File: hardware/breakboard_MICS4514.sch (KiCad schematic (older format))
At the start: 11 parts, among them J1 outputs, Q1 2N7002, U1 TLC2272, U2 MICS-4514

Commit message: shape of edge cuts
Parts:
- removed J1: outputs, Connector_PinHeader_2.54mm:PinHeader_1x07_P2.54mm_Vertical, symbol Connector:Conn_01x07_Female
- added J1: OUTPUTS, Connector_PinHeader_2.54mm:PinHeader_1x05_P2.54mm_Vertical, symbol Connector:Conn_01x05_Female
- R5: value 22k -> 269
- U2: symbol electroniccats:MICS-4514 -> breakboard_MICS4514-rescue:MICS-4514-electroniccats
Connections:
- wire segments 55 -> 50
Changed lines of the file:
@@
 EESchema Schematic File Version 4
 LIBS:breakboard_MICS4514-cache
-EELAYER 26 0
+EELAYER 29 0
 EELAYER END
 $Descr A4 11693 8268
@@
 $EndDescr
 $Comp
-L electroniccats:MICS-4514 U2
+L breakboard_MICS4514-rescue:MICS-4514-electroniccats U2
 U 1 1 5C5C9644
 P 6730 2780
@@
 P 5190 3310
 F 0 "R5" H 5260 3356 50  0000 L CNN
-F 1 "22k" H 5260 3265 50  0000 L CNN
+F 1 "269" H 5260 3265 50  0000 L CNN
 F 2 "Resistor_SMD:R_0805_2012Metric_Pad1.15x1.40mm_HandSolder" V 5120 3310 50  0001 C CNN
 F 3 "https://www.mouser.mx/datasheet/2/348/esr-e-1139161.pdf" H 5190 3310 50  0001 C CNN
@@
 	6980 5040 7080 5040
 $Comp
-L Connector:Conn_01x07_Female J1
-U 1 1 5C5D8712
-P 7760 3800
-F 0 "J1" H 7788 3826 50  0000 L CNN
-F 1 "outputs" H 7788 3735 50  0000 L CNN
-F 2 "Connector_PinHeader_2.54mm:PinHeader_1x07_P2.54mm_Vertical" H 7760 3800 50  0001 C CNN
-F 3 "~" H 7760 3800 50  0001 C CNN
-	1    7760 3800
-	1    0    0    -1
-$EndComp
-$Comp
 L power:+3V3 #PWR08
 U 1 1 5C5D9752
-P 6830 3420
-F 0 "#PWR08" H 6830 3270 50  0001 C CNN
-F 1 "+3V3" H 6845 3593 50  0000 C CNN
-F 2 "" H 6830 3420 50  0001 C CNN
-F 3 "" H 6830 3420 50  0001 C CNN
-	1    6830 3420
+P 7070 3640
+F 0 "#PWR08" H 7070 3490 50  0001 C CNN
+F 1 "+3V3" H 7085 3813 50  0000 C CNN
+F 2 "" H 7070 3640 50  0001 C CNN
+F 3 "" H 7070 3640 50  0001 C CNN
+	1    7070 3640
 	1    0    0    -1
 $EndComp
@@
 L power:GND #PWR07
 U 1 1 5C5D97A5
-P 6830 3740
-F 0 "#PWR07" H 6830 3490 50  0001 C CNN
-F 1 "GND" H 6835 3567 50  0000 C CNN
-F 2 "" H 6830 3740 50  0001 C CNN
-F 3 "" H 6830 3740 50  0001 C CNN
-	1    6830 3740
-	1    0    0    -1
-$EndComp
-Text Label 7460 3600 2    50   ~ 0
+P 7070 3820
+F 0 "#PWR07" H 7070 3570 50  0001 C CNN
+F 1 "GND" H 7075 3647 50  0000 C CNN
+F 2 "" H 7070 3820 50  0001 C CNN
+F 3 "" H 7070 3820 50  0001 C CNN
+	1    7070 3820
+	1    0    0    -1
+$EndComp
+Text Label 7310 4100 2    50   ~ 0
 PRE_HEALTING
-Text Label 7460 3800 2    50   ~ 0
-OX
-Text Label 7460 3900 2    50   ~ 0
-RED
-Text Label 7460 4100 2    50   ~ 0
+Text Label 7310 4000 2    50   ~ 0
 NO2
-Text Label 7460 4000 2    50   ~ 0
+Text Label 7310 3900 2    50   ~ 0
 CO2
 Wire Wire Line
-	7460 3600 7560 3600
-Wire Wire Line
-	7460 3800 7560 3800
-Wire Wire Line
-	7460 3900 7560 3900
-Wire Wire Line
-	7460 4000 7560 4000
-Wire Wire Line
-	7460 4100 7560 4100
-Wire Wire Line
 	5190 3820 5190 3460
 Wire Wire Line
 	4870 3820 4870 3460
-Wire Wire Line
-	6830 3740 6830 3700
-Wire Wire Line
-	6830 3700 7560 3700
-Wire Wire Line
-	7560 3500 6830 3500
-Wire Wire Line
-	6830 3500 6830 3420
 Text Label 6080 4940 2    50   ~ 0
 RED
+$Comp
+L Connector:Conn_01x05_Female J1
+U 1 1 5CFFB1C2
+P 7510 3900
+F 0 "J1" H 7538 3926 50  0000 L CNN
+F 1 "OUTPUTS" H 7538 3835 50  0000 L CNN
+F 2 "Connector_PinHeader_2.54mm:PinHeader_1x05_P2.54mm_Vertical" H 7510 3900 50  0001 C CNN
+F 3 "~" H 7510 3900 50  0001 C CNN
+	1    7510 3900
+	1    0    0    -1
+$EndComp
+Wire Wire Line
+	7070 3640 7070 3700
+Wire Wire Line
+	7070 3700 7310 3700
+Wire Wire Line
+	7310 3800 7070 3800
+Wire Wire Line
+	7070 3800 7070 3820
 $EndSCHEMATC

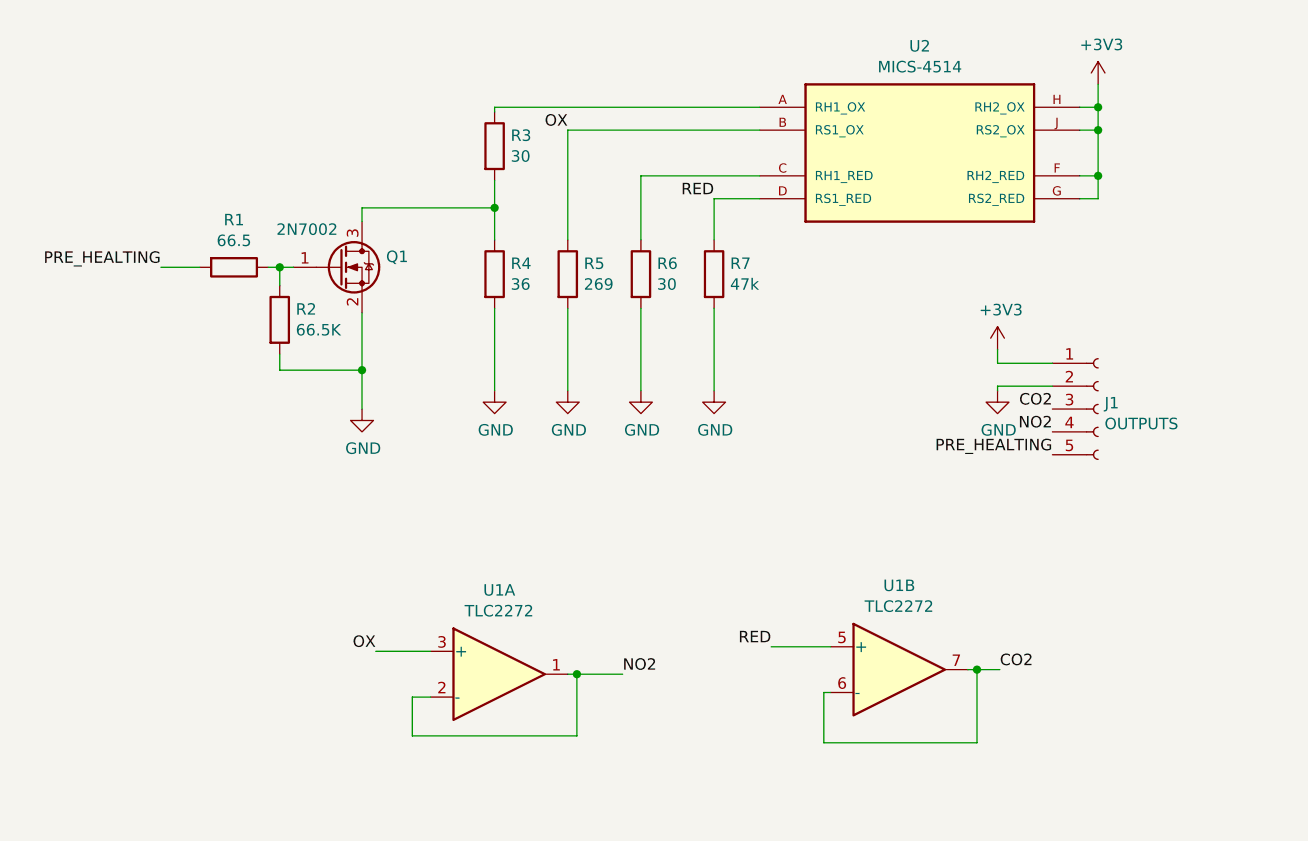
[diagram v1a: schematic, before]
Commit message: Add voltage pins for opamp, add decoupling caps, new component placement
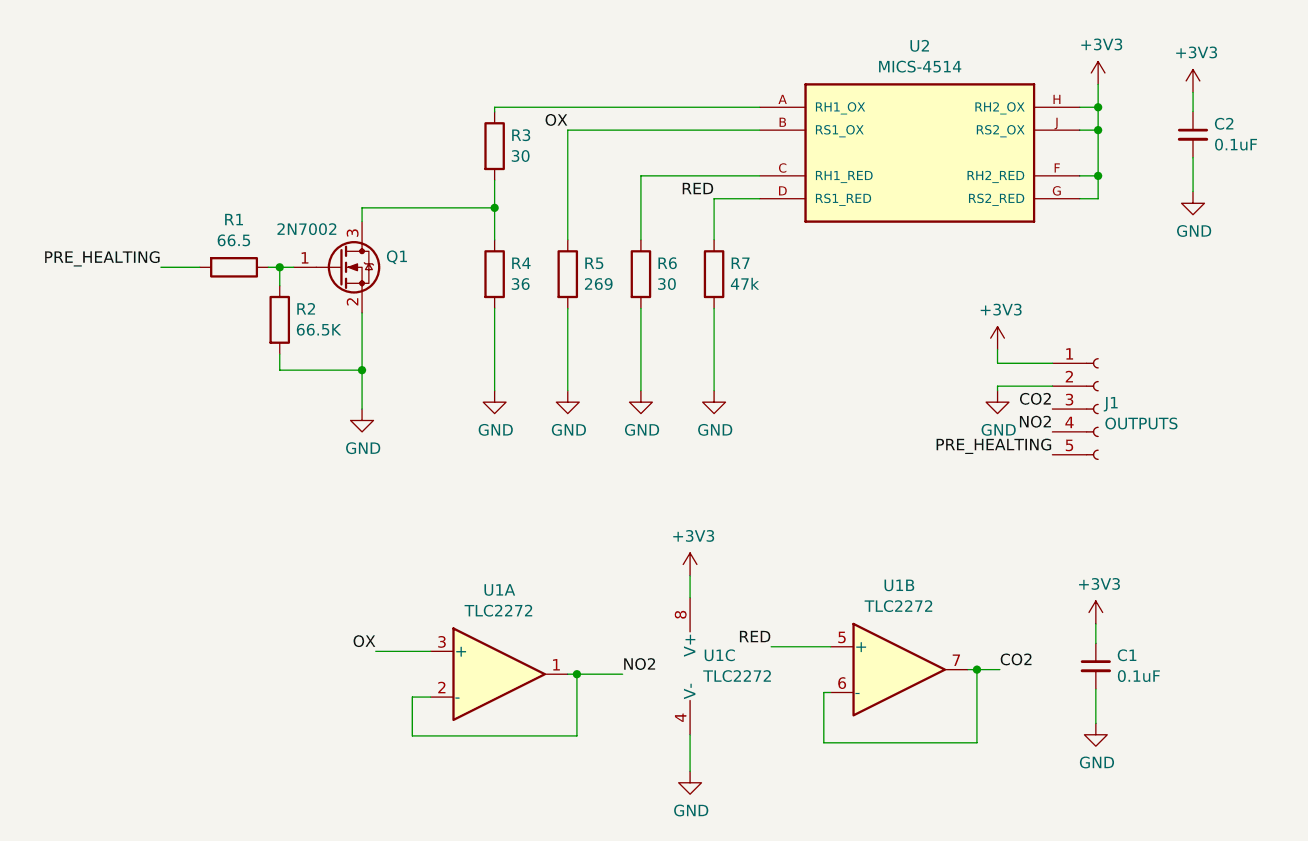
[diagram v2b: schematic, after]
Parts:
- added C1, C2: 0.1uF, Capacitor_SMD:C_0805_2012Metric_Pad1.15x1.40mm_HandSolder, symbol Device:C_Small
- added unit 3 of U1
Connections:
- net +3V3: now also C1.1, C2.1, U1.8 (V+)
- net GND: now also C1.2, C2.2, U1.4 (V-)
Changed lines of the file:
@@
 EESchema Schematic File Version 4
-LIBS:breakboard_MICS4514-cache
-EELAYER 29 0
+EELAYER 30 0
 EELAYER END
 $Descr A4 11693 8268
@@
 Sheet 1 1
 Title "Breakboard MICS4514"
-Date "2019-02-07"
-Rev ""
-Comp "ELECTRONIC CATS "
+Date "2020-04-24"
+Rev "v1.0"
+Comp "Electronic Cats"
 Comment1 "ROCIO RODRIGUEZ"
-Comment2 ""
+Comment2 "Eduardo Contreras"
 Comment3 ""
 Comment4 ""
@@
 F 4 "CRCW080530R0FKEAC" H 5510 3310 50  0001 C CNN "manf#"
 	1    5510 3310
-	1    0    0    -1
-$EndComp
-$Comp
-L Amplifier_Operational:TLC272 U1
-U 1 1 5C5C9A60
-P 4890 5060
-F 0 "U1" H 4890 5427 50  0000 C CNN
-F 1 "TLC2272" H 4890 5336 50  0000 C CNN
-F 2 "Package_SO:SOIC-8_3.9x4.9mm_P1.27mm" H 4890 5060 50  0001 C CNN
-F 3 "http://www.ti.com/lit/ds/symlink/tlc2272.pdf" H 4890 5060 50  0001 C CNN
-F 4 "TLC2272CD" H 4890 5060 50  0001 C CNN "manf#"
-	1    4890 5060
-	1    0    0    -1
-$EndComp
-$Comp
-L Amplifier_Operational:TLC272 U1
-U 2 1 5C5C9ABF
-P 6640 5040
-F 0 "U1" H 6640 5407 50  0000 C CNN
-F 1 "TLC2272" H 6640 5316 50  0000 C CNN
-F 2 "Package_SO:SOIC-8_3.9x4.9mm_P1.27mm" H 6640 5040 50  0001 C CNN
-F 3 "http://www.ti.com/lit/ds/symlink/tlc2272.pdf" H 6640 5040 50  0001 C CNN
-F 4 "TLC2272CD" H 10  600 50  0001 C CNN "manf#"
-	2    6640 5040
 	1    0    0    -1
 $EndComp
@@
 Wire Wire Line
 	7070 3800 7070 3820
+$Comp
+L Amplifier_Operational:TLC272 U1
+U 1 1 5C5C9A60
+P 4890 5060
+F 0 "U1" H 4890 5427 50  0000 C CNN
+F 1 "TLC2272" H 4890 5336 50  0000 C CNN
+F 2 "Package_SO:SOIC-8_3.9x4.9mm_P1.27mm" H 4890 5060 50  0001 C CNN
+F 3 "http://www.ti.com/lit/ds/symlink/tlc2272.pdf" H 4890 5060 50  0001 C CNN
+F 4 "TLC2272CD" H 4890 5060 50  0001 C CNN "manf#"
+	1    4890 5060
+	1    0    0    -1
+$EndComp
+$Comp
+L Amplifier_Operational:TLC272 U1
+U 2 1 5C5C9ABF
+P 6640 5040
+F 0 "U1" H 6640 5407 50  0000 C CNN
+F 1 "TLC2272" H 6640 5316 50  0000 C CNN
+F 2 "Package_SO:SOIC-8_3.9x4.9mm_P1.27mm" H 6640 5040 50  0001 C CNN
+F 3 "http://www.ti.com/lit/ds/symlink/tlc2272.pdf" H 6640 5040 50  0001 C CNN
+F 4 "TLC2272CD" H 10  600 50  0001 C CNN "manf#"
+	2    6640 5040
+	1    0    0    -1
+$EndComp
+$Comp
+L Amplifier_Operational:LM2904 U1
+U 3 1 5EA41EC3
+P 5825 5025
+F 0 "U1" H 5783 5071 50  0000 L CNN
+F 1 "TLC2272" H 5783 4980 50  0000 L CNN
+F 2 "Package_SO:SOIC-8_3.9x4.9mm_P1.27mm" H 5825 5025 50  0001 C CNN
+F 3 "http://www.ti.com/lit/ds/symlink/tlc2272.pdf" H 5825 5025 50  0001 C CNN
+	3    5825 5025
+	1    0    0    -1
+$EndComp
+$Comp
+L power:+3V3 #PWR09
+U 1 1 5EA54096
+P 5725 4630
+F 0 "#PWR09" H 5725 4480 50  0001 C CNN
+F 1 "+3V3" H 5740 4803 50  0000 C CNN
+F 2 "" H 5725 4630 50  0001 C CNN
+F 3 "" H 5725 4630 50  0001 C CNN
+	1    5725 4630
+	1    0    0    -1
+$EndComp
+Wire Wire Line
+	5725 4630 5725 4725
+$Comp
+L power:GND #PWR012
+U 1 1 5EA5A6B2
+P 5725 5485
+F 0 "#PWR012" H 5725 5235 50  0001 C CNN
+F 1 "GND" H 5730 5312 50  0000 C CNN
+F 2 "" H 5725 5485 50  0001 C CNN
+F 3 "" H 5725 5485 50  0001 C CNN
+	1    5725 5485
+	1    0    0    -1
+$EndComp
+Wire Wire Line
+	5725 5485 5725 5325
+$Comp
+L Device:C_Small C1
+U 1 1 5EA5E613
+P 7500 5025
+F 0 "C1" H 7592 5071 50  0000 L CNN
+F 1 "0.1uF" H 7592 4980 50  0000 L CNN
+F 2 "Capacitor_SMD:C_0805_2012Metric_Pad1.15x1.40mm_HandSolder" H 7500 5025 50  0001 C CNN
+F 3 "~" H 7500 5025 50  0001 C CNN
+	1    7500 5025
+	1    0    0    -1
+$EndComp
+$Comp
+L power:+3V3 #PWR010
+U 1 1 5EA5FC47
+P 7500 4840
+F 0 "#PWR010" H 7500 4690 50  0001 C CNN
+F 1 "+3V3" H 7515 5013 50  0000 C CNN
+F 2 "" H 7500 4840 50  0001 C CNN
+F 3 "" H 7500 4840 50  0001 C CNN
+	1    7500 4840
+	1    0    0    -1
+$EndComp
+Wire Wire Line
+	7500 4840 7500 4925
+$Comp
+L power:GND #PWR011
+U 1 1 5EA61FB4
+P 7500 5275
+F 0 "#PWR011" H 7500 5025 50  0001 C CNN
+F 1 "GND" H 7505 5102 50  0000 C CNN
+F 2 "" H 7500 5275 50  0001 C CNN
+F 3 "" H 7500 5275 50  0001 C CNN
+	1    7500 5275
+	1    0    0    -1
+$EndComp
+Wire Wire Line
+	7500 5125 7500 5275
+$Comp
+L Device:C_Small C2
+U 1 1 5EA37C23
+P 7925 2700
+F 0 "C2" H 8017 2746 50  0000 L CNN
+F 1 "0.1uF" H 8017 2655 50  0000 L CNN
+F 2 "Capacitor_SMD:C_0805_2012Metric_Pad1.15x1.40mm_HandSolder" H 7925 2700 50  0001 C CNN
+F 3 "~" H 7925 2700 50  0001 C CNN
+	1    7925 2700
+	1    0    0    -1
+$EndComp
+$Comp
+L power:+3V3 #PWR013
+U 1 1 5EA37C2D
+P 7925 2515
+F 0 "#PWR013" H 7925 2365 50  0001 C CNN
+F 1 "+3V3" H 7940 2688 50  0000 C CNN
+F 2 "" H 7925 2515 50  0001 C CNN
+F 3 "" H 7925 2515 50  0001 C CNN
+	1    7925 2515
+	1    0    0    -1
+$EndComp
+Wire Wire Line
+	7925 2515 7925 2600
+$Comp
+L power:GND #PWR014
+U 1 1 5EA37C38
+P 7925 2950
+F 0 "#PWR014" H 7925 2700 50  0001 C CNN
+F 1 "GND" H 7930 2777 50  0000 C CNN
+F 2 "" H 7925 2950 50  0001 C CNN
+F 3 "" H 7925 2950 50  0001 C CNN
+	1    7925 2950
+	1    0    0    -1
+$EndComp
+Wire Wire Line
+	7925 2800 7925 2950
 $EndSCHEMATC
